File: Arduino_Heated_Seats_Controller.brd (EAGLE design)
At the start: 32.7 x 36.8 mm, 28 parts, among them U1 MEGA8-AI, U3 ULN2003ADE4, U4 IC_TD62783-SO-18W

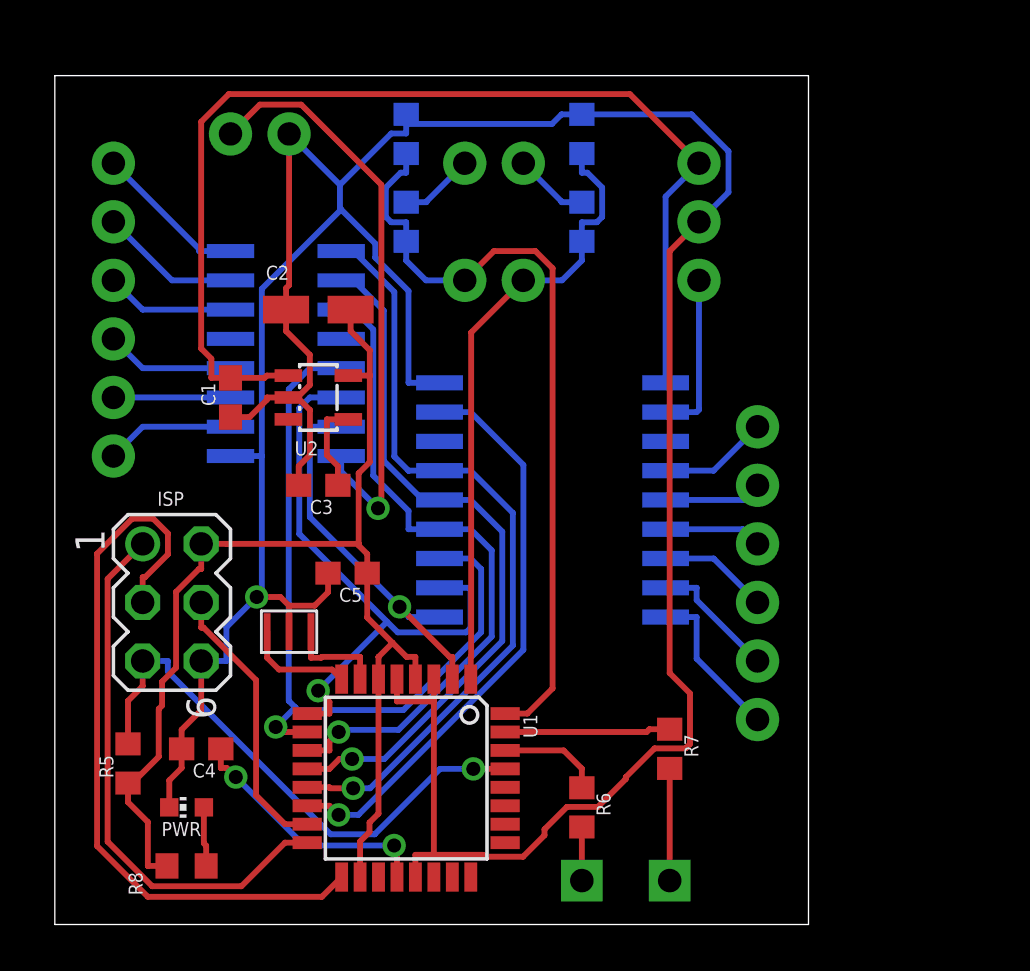
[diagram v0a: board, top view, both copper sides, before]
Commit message: A few more layout changes to accommodate part changes and physical part dimensions. Still a few more things to add (drills for mounting, traces to widen, silk to add) but nothing major.
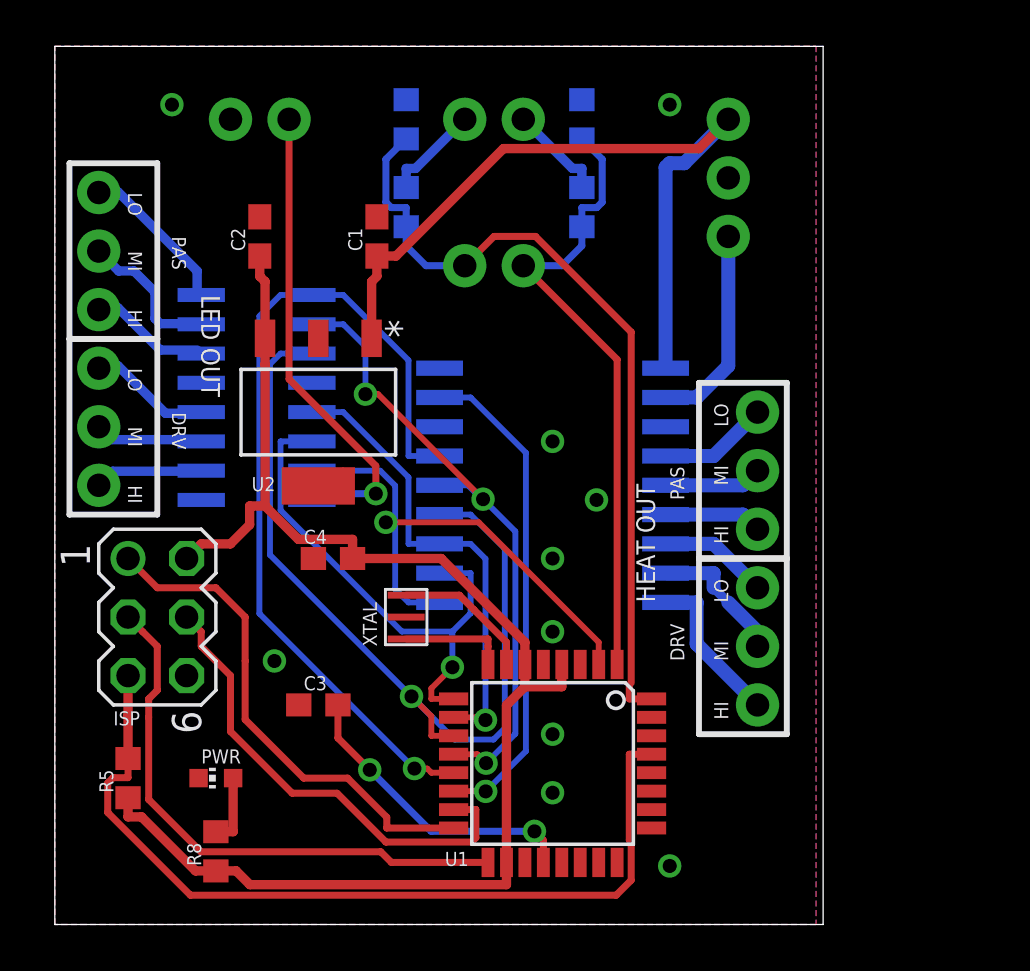
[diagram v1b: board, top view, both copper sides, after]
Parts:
- removed C5: 0.1uF, rcl:C0603
- removed R6, R7: 1k, resistor:R0603
- removed RXI, TXO: PAD_TERMINAL-1.02MM_SQUARE, dp_devices:CON_PAD_SQUARE_1.02MM
- C1: value 0.1uF -> 0.33uF
- C2: device rcl:CT3216 -> rcl:C0603
- C3: value 470pF -> 0.1uF
- U2: value (none) -> UA78M05CDCY; device v-reg-micrel:SOT23-5 -> Texas Instruments_By_element14_Batch_1:SOT230P700X180-4N
- moved C4 10.0 mm to (12.1, 15.9)
- moved C3 9.53 mm to (11.4, 9.53)
- moved C1 9.44 mm to (14.0, 29.8), turned to 90 degrees
- moved U1 6.38 mm to (21.6, 6.99)
- moved XTAL 5.12 mm to (15.2, 13.3), turned to 270 degrees
- moved C2 4.07 mm to (8.89, 29.8), turned to 90 degrees
- moved LED-TEST 2.62 mm to (10.2, 34.9), turned to 0 degrees
- moved U3 2.29 mm to (6.35, 18.4)
- moved PWR/H 2.29 mm to (29.2, 34.9)
- moved BTN-IN 1.90 mm to (17.8, 34.9)
- moved PWR 1.80 mm to (6.99, 6.35)
- moved R8 1.42 mm to (6.99, 3.17), turned to 90 degrees
- moved LED-OUT 1.42 mm to (1.91, 19.1)
- moved ISP 0.90 mm to (4.45, 13.3)
- moved R5 0.64 mm to (3.17, 6.35)
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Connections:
- net PB0/D8 renamed D8
- net PB1/D9 renamed D9
- net PB2/D10 renamed D10
- net PB3/D11 renamed D11
- net PB4/D12 renamed D12
- net PB5/D13 renamed D13
- net PD2/D2 renamed D2
- net PD3/D3 renamed D3
- net PD4/D4 renamed D4
- net PD5/D5 renamed D5
- net PD6/D6 renamed D6
- net PD7/D7 renamed D7
- removed net ADC0/A0: U1.23
- removed net ADC1/A1: U1.24
- removed net ADC2/A2: U1.25
- removed net ADC3/A3: U1.26
- removed net ADC4/A4/SDA: U1.27
- removed net ADC5/A5/SCL: U1.28
- removed net ADC6/A6: U1.19
- removed net ADC7/A7: U1.22
- removed net EN: U2.3
- removed net N$4: C3.1, U2.4
- removed net N$8: R6.1, U1.30
- removed net N$9: R7.1, U1.31
- removed net RXI: R6.2, RXI.P
- removed net TXO: R7.2, TXO.P
- net AREF: now also C3.1; no longer C4.1
- net GND: now also C2.2, U2.4; no longer C2.-, C5.2
- net VDD: now also C2.1, C4.1, U2.3; no longer C2.+, C5.1, U2.5
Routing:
- net GND: track 142.3 -> 0.00 mm, vias 1 -> 10
- net VIN: track 48.1 -> 33.7 mm
- net RESET: track 24.1 -> 37.6 mm, vias 1 -> 0
- net D6: track 33.5 -> 20.3 mm
- net D7: track 29.1 -> 38.2 mm
- net VDD: track 53.0 -> 61.8 mm
- net D11: track 12.1 -> 20.6 mm
- net D13: track 32.0 -> 24.4 mm
- net N$9: track 7.19 -> 0.00 mm
- net D4: track 16.9 -> 23.3 mm
- net TXO: track 4.86 -> 0.00 mm
- net L-TEST: track 25.5 -> 20.7 mm
- net N$8: track 4.48 -> 0.00 mm
- net D9: track 33.6 -> 37.7 mm
- net N$4: track 3.99 -> 0.00 mm
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- added copper zone on layer 1, net GND
- added copper zone on layer 16, net GND
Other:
- board size 32.7 x 36.8 mm -> 33.3 x 38.1 mm
- board text added: "DRV"
- board text added: "HEAT OUT"
- board text added: "HI"
- board text added: "LED OUT"
- board text added: "LO"
- board text added: "MI"
- board text added: "PAS"
- board text added: "XTAL"

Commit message: More tweaks to traces (hopefully final). More silk labels (on pins as well). Holes (for mounting). And anything else I might have forgotten - looks ready to send to fab for electrical test.
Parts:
- added U$1: (no value), Logo:OSHW_FILLX100_NOTEXT
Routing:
- net D3: track 27.6 -> 28.7 mm
- net D2: track 35.0 -> 36.1 mm
- net D-BTN: track 4.25 -> 5.25 mm
- net P-BTN: track 4.25 -> 5.25 mm
- net PL-MID: track 6.95 -> 6.15 mm
- net VIN: track 33.7 -> 34.4 mm
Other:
- board size 33.3 x 38.1 mm -> 32.7 x 38.1 mm
- board text added: "+"
- board text added: "-"
- board text added: "Arduino Powered Heated Seat Controller rev. 3"
- board text added: "C"
- board text added: "H"
- board text added: "https://github.com/avluis/ArduinoHeatedSeatController-Hardware"

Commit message: Changes so far - commit before tweaking trace width and misc.
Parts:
- removed BTN-TEST, LED-TEST: (no value), SparkFun-Connectors:1X02
- U$1: device Logo:OSHW_FILLX100_NOTEXT -> Logo:OSHW_10X500_NOTEXT
- moved LED-OUT 36.2 mm to (38.1, 21.0)
- moved U3 25.2 mm to (31.5, 18.9), flipped to the top
- moved U$1 20.6 mm to (26.0, 14.0), flipped to the bottom
- moved U4 11.6 mm to (28.3, 8.95), flipped to the top, turned to 270 degrees
- moved C4 11.5 mm to (23.5, 17.5), turned to 90 degrees
- moved H-OUT 11.2 mm to (38.1, 17.8), turned to 270 degrees
- moved C3 10.0 mm to (8.26, 19.1), turned to 90 degrees
- moved U1 8.64 mm to (14.6, 12.1), turned to 180 degrees
- moved C1 7.65 mm to (6.35, 30.5)
- moved XTAL 7.10 mm to (20.4, 18.2), turned to 90 degrees
- moved U2 7.01 mm to (4.45, 22.9)
- moved C2 6.38 mm to (2.54, 30.5)
- moved R1 6.35 mm to (11.4, 26.0), flipped to the top, turned to 180 degrees
- moved R2 6.35 mm to (19.1, 26.0), flipped to the top, turned to 0 degrees
- moved R3 6.29 mm to (10.8, 30.5), flipped to the top
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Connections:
- removed net L-TEST: LED-TEST.1, U3.8
- net D2: no longer BTN-TEST.1
- net D3: no longer BTN-TEST.2
- net GND: now also U3.8; no longer LED-TEST.2, U3.9
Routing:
- net VIN: track 34.4 -> 65.9 mm
- net H-ON: track 8.90 -> 31.3 mm, vias 0 -> 1
- net L-TEST: track 20.7 -> 0.00 mm, vias 1 -> 0
- net RESET: track 37.5 -> 22.2 mm
- net D13: track 24.4 -> 10.5 mm
- net D2: track 36.1 -> 49.4 mm
- net D6: track 20.3 -> 29.7 mm, vias 1 -> 0
- net D12: track 21.8 -> 13.9 mm
- net D4: track 23.3 -> 16.3 mm, vias 1 -> 0
- net D9: track 37.7 -> 43.8 mm, vias 1 -> 0
- net D11: track 20.6 -> 25.5 mm
- net AREF: track 13.1 -> 8.44 mm, vias 2 -> 0
- net D10: track 21.5 -> 17.0 mm, vias 1 -> 0
- net D5: track 22.4 -> 25.6 mm, vias 1 -> 0
- net D-BTN: track 5.25 -> 8.32 mm
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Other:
- board size 32.7 x 38.1 mm -> 40.3 x 35.5 mm
- board text added: "Arduino Powered Heated Seat Controller rev. 4"
- board text removed: "Arduino Powered Heated Seat Controller rev. 3"
- board text removed: "C"

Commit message: Final tweaks and changes - off to the fab house.
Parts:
- moved C3 6.87 mm to (8.64, 12.2), turned to 270 degrees
- moved C1 6.12 mm to (9.46, 25.2), turned to 270 degrees
- moved R1 3.59 mm to (14.0, 28.6), turned to 270 degrees
- moved R2 3.59 mm to (16.5, 28.6), turned to 270 degrees
- moved U$1 3.24 mm to (28.1, 11.5)
- moved R3 2.03 mm to (11.5, 28.6)
- moved R4 2.03 mm to (19.0, 28.6)
- moved XTAL 1.41 mm to (21.2, 17.1)
- moved R8 0.97 mm to (9.27, 4.83), turned to 0 degrees
- moved H-OUT 0.89 mm to (38.2, 16.9)
- moved BTN-IN 0.83 mm to (14.0, 32.8)
- moved R5 0.74 mm to (5.71, 4.83), turned to 180 degrees
- moved PWR/H 0.71 mm to (24.9, 33.0)
- moved LED-OUT 0.70 mm to (38.2, 20.3)
- moved C4 0.46 mm to (23.9, 17.2)
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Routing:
- net D10: track 17.0 -> 50.3 mm
- net D8: track 29.0 -> 40.1 mm, vias 2 -> 0
- net AREF: track 8.44 -> 2.21 mm
- net P-BTN: track 8.32 -> 3.43 mm
- net D-BTN: track 8.32 -> 3.43 mm
- net VIN: track 65.9 -> 61.7 mm, vias 0 -> 1
- net D3: track 27.5 -> 24.0 mm
- net D11: track 25.5 -> 22.1 mm
- net D2: track 49.4 -> 51.9 mm
- net H-ON: track 31.3 -> 33.7 mm
- net D4: track 16.3 -> 18.6 mm
- net D12: track 13.9 -> 11.6 mm
- net N$3: track 2.99 -> 4.21 mm
- net D9: track 43.8 -> 44.6 mm
- net DH-HIGH: track 7.21 -> 6.45 mm
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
